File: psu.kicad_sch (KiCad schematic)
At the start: 30 parts, among them U7 LM2593HVS-ADJ, U8 LM2575S-5, U9 LM2575S-3.3

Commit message: More updates to regularise property names
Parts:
- C25: Manuf (none) -> Samsung Electro-Mechanics; Mfr Samsung Electro-Mechanics -> (none); Mfr Part No CL21A475KBQNNNE -> (none); Part (none) -> CL21A475KBQNNNE; Supl Mouser -> (none); Supl Part No 187-CL21A475KBQNNNE -> (none); Supl Price 0.20 -> (none); Vendor (none) -> Mouser; Vendor Cost (none) -> 0.20; Vendor SKU (none) -> 187-CL21A475KBQNNNE
- C26, C27, C28, C50: Manuf (none) -> Samsung Electro-Mechanics; Mfr Samsung Electro-Mechanics -> (none); Mfr Name C0402C104K8R7411 -> (none); Mfr Part Mouser -> (none); Mfr Part No CL21B104KACNNND -> (none); Part 0.016 -> CL21B104KACNNND; Price KEMET -> (none); Repr-Cost C0402C104K8R7411 -> (none); Stock Number Mouser -> (none); Supl Mouser -> (none); Supl Part No 187-CL21B104KACNNND -> (none); Supl Price 0.027 -> (none); Vendor (none) -> Mouser; Vendor Cost (none) -> 0.027; Vendor SKU (none) -> 187-CL21B104KACNNND
- C29, C32, C33: Manuf (none) -> Samsung Electro-Mechanics; Mfr Samsung Electro-Mechanics -> (none); Mfr Part No CL21A475KAQNNNG -> (none); Part (none) -> CL21A475KAQNNNG; Supl Mouser -> (none); Supl Part No 187-CL21A475KAQNNNG -> (none); Supl Price 0.092 -> (none); Vendor (none) -> Mouser; Vendor Cost (none) -> 0.092; Vendor SKU (none) -> 187-CL21A475KAQNNNG
- C30, C31: Manuf (none) -> CDE / Illinois Capacitor; Mfr CDE / Illinois Capacitor -> (none); Mfr Name 476KXM050M -> (none); Mfr Part Mouser -> (none); Mfr Part No 476KXM050M -> (none); Part 0.269 -> 476KXM050M; Price CDE / Illinois Capacitor -> (none); Repr-Cost 476KXM050M -> (none); Stock Number Mouser -> (none); Supl Mouser -> (none); Supl Part No 598-476KXM050M -> (none); Supl Price 0.269 -> (none); Vendor (none) -> Mouser; Vendor Cost (none) -> 0.269; Vendor SKU (none) -> 598-476KXM050M
- C34: Manuf (none) -> Samsung Electro-Mechanics; Mfr Samsung Electro-Mechanics -> (none); Mfr Part No 187-CL31A476MQHNNNE -> (none); Part (none) -> CL31A476MQHNNNE; Supl Mouser -> (none); Supl Part No 187-CL31A476MQHNNNE -> (none); Supl Price 0.262 -> (none); Vendor (none) -> Mouser; Vendor Cost (none) -> 0.262; Vendor SKU (none) -> 187-CL31A476MQHNNNE
- C49: Manuf (none) -> Taiyo Yuden; Mfr Taiyo Yuden -> (none); Mfr Name C0402C104K8R7411 -> (none); Mfr Part Mouser -> (none); Mfr Part No EMK212BJ105KG-T -> (none); Part Mouser -> EMK212BJ105KG-T; Price 80-C0402C104K8R7411 -> (none); Repr-Cost 0.016 -> (none); Stock Number C0402C104K8R7411 -> (none); Supl Mouser -> (none); Supl Part No 963-EMK212BJ105KG-T -> (none); Supl Price 0.016 -> (none); Vendor (none) -> Mouser; Vendor Cost (none) -> 0.016; Vendor SKU (none) -> 963-EMK212BJ105KG-T
- CP3: Manuf (none) -> Nichicon; Mfr Nichicon -> (none); Mfr Part No UPJ1H471MHD -> (none); Part (none) -> UPJ1H471MHD; Supl Mouser -> (none); Supl Part No 647-UPJ1H471MHD -> (none); Supl Price 0.793 -> (none); Vendor (none) -> Mouser; Vendor Cost (none) -> 0.793; Vendor SKU (none) -> 647-UPJ1H471MHD
- CP4: Manuf (none) -> Nichicon; Mfr Nichicon -> (none); Mfr Part No UPJ1E471MPD -> (none); Part (none) -> UPJ1E471MPD; Supl Mouser -> (none); Supl Part No 647-UPJ1E471MPD -> (none); Supl Price 0.549 -> (none); Vendor (none) -> Mouser; Vendor Cost (none) -> 0.549; Vendor SKU (none) -> 647-UPJ1E471MPD
- CP5, CP6: Manuf (none) -> Nichicon; Mfr Nichicon -> (none); Mfr Part No UPJ1A391MPD6 -> (none); Part (none) -> UPJ1A391MPD6; Supl Mouser -> (none); Supl Part No 647-UPJ1A391MPD6 -> (none); Supl Price 0.465 -> (none); Vendor (none) -> Mouser; Vendor Cost (none) -> 0.465; Vendor SKU (none) -> 647-UPJ1A391MPD6
- CP8: Manuf (none) -> YAGEO; Mfr YAGEO -> (none); Mfr Part No SK050M047AZS0611 -> (none); Part (none) -> SK050M047AZS0611; Supl Mouser -> (none); Supl Part No 603-SK050M047AZS0611 -> (none); Supl Price 0.122 -> (none); Vendor (none) -> Mouser; Vendor Cost (none) -> 0.122; Vendor SKU (none) -> 603-SK050M047AZS0611
- D13: Manuf (none) -> Vishay; Manuf Part No PLZ3V6A-G3/H -> (none); Manufacturer Vishay -> (none); Mfr Vishay -> (none); Mfr Part No PLZ3V6A-G3/H -> (none); Part (none) -> PLZ3V6A-G3/H; Supl Mouser -> (none); Supl Part No 78-PLZ3V6A-G3/H -> (none); Supl Price 0.23 -> (none); Supplier Mouser -> (none); Vendor (none) -> Mouser; Vendor Cost (none) -> 0.23; Vendor SKU (none) -> 78-PLZ3V6A-G3/H
- D6: value B140-E3/5AT -> B140-E3; Manuf (none) -> Vishay; Mfr Vishay -> (none); Mfr Part No B140-E3/5AT -> (none); Part (none) -> B140-E3/5AT; Supl Mouser -> (none); Supl Part No 625-B140-E3 -> (none); Supl Price 0.277 -> (none); Vendor (none) -> Mouser; Vendor Cost (none) -> 0.277; Vendor SKU (none) -> 625-B140-E3
- D7, D8: value B140-E3/5AT -> B140-E3; Manuf (none) -> Vishay; Mfr Vishay -> (none); Mfr Part No B140-E3 -> (none); Part (none) -> B140-E3/5AT; Supl Mouser -> (none); Supl Part No 625-B140-E3 -> (none); Supl Price 0.277 -> (none); Vendor (none) -> Mouser; Vendor Cost (none) -> 0.277; Vendor SKU (none) -> 625-B140-E3
- L2: Manuf (none) -> Coilcraft; Mfr Coilcraft -> (none); Mfr Part No MSS1278H-683KED -> (none); Part (none) -> MSS1278H-683KED; Supl Mouser -> (none); Supl Part No 994-MSS1278H-683KED -> (none); Supl Price 2.13 -> (none); Vendor (none) -> Mouser; Vendor Cost (none) -> 2.13; Vendor SKU (none) -> 994-MSS1278H-683KED
- L3, L4: Manuf (none) -> Coilcraft; Mfr Coilcraft -> (none); Mfr Part No MSS1038-104MLC -> (none); Part (none) -> MSS1038-104MLC; Supl Mouser -> (none); Supl Part No 994-MSS1038-104MLC -> (none); Supl Price 1.32 -> (none); Vendor (none) -> Mouser; Vendor Cost (none) -> 1.32; Vendor SKU (none) -> 994-MSS1038-104MLC
- R20: Manuf (none) -> Yageo; Mfr Yageo -> (none); Mfr Part No RC0805FR-134K7L -> (none); Part (none) -> RC0805FR-134K7L; Supl Mouser -> (none); Supl Part No 603-RC0805FR-134K7L -> (none); Supl Price 0.077 -> (none); Vendor (none) -> Mouser; Vendor Cost (none) -> 0.077; Vendor SKU (none) -> 603-RC0805FR-134K7L
- R21, R22: Manuf (none) -> KOA Speer; Mfr KOA Speer -> (none); Mfr Part No RN732ATTD2182D25 -> (none); Part (none) -> RN732ATTD2182D25; Supl Mouser -> (none); Supl Part No 660-RN732ATTD2182D25 -> (none); Supl Price 0.33 -> (none); Vendor (none) -> Mouser; Vendor Cost (none) -> 0.33; Vendor SKU (none) -> 660-RN732ATTD2182D25
- U7: Manuf (none) -> TI; Mfr TI -> (none); Mfr Part No LM2593HVSX-ADJ/NOPB -> (none); Part (none) -> LM2593HVSX-ADJ/NOPB; Supl Mouser -> (none); Supl Part No 926-LM2593HVSXADJNPB -> (none); Supl Price 5.44 -> (none); Vendor (none) -> Mouser; Vendor Cost (none) -> 5.44; Vendor SKU (none) -> 926-LM2593HVSXADJNPB
- U8: Manuf (none) -> onsemi; Mfr onsemi -> (none); Mfr Part No LM2575D2T-5G -> (none); Part (none) -> LM2575D2T-5G; Supl Mouser -> (none); Supl Part No 863-LM2575D2T-5G -> (none); Supl Price 1.99 -> (none); Vendor (none) -> Mouser; Vendor Cost (none) -> 1.99; Vendor SKU (none) -> 863-LM2575D2T-5G
- U9: Manuf (none) -> onsemi; Mfr onsemi -> (none); Mfr Part No LM2575T-3.3G -> (none); Part (none) -> LM2575T-3.3G; Supl Mouser -> (none); Supl Part No 863-LM2575T-3.3G -> (none); Supl Price 1.76 -> (none); Vendor (none) -> Mouser; Vendor Cost (none) -> 1.76; Vendor SKU (none) -> 863-LM2575T-3.3G

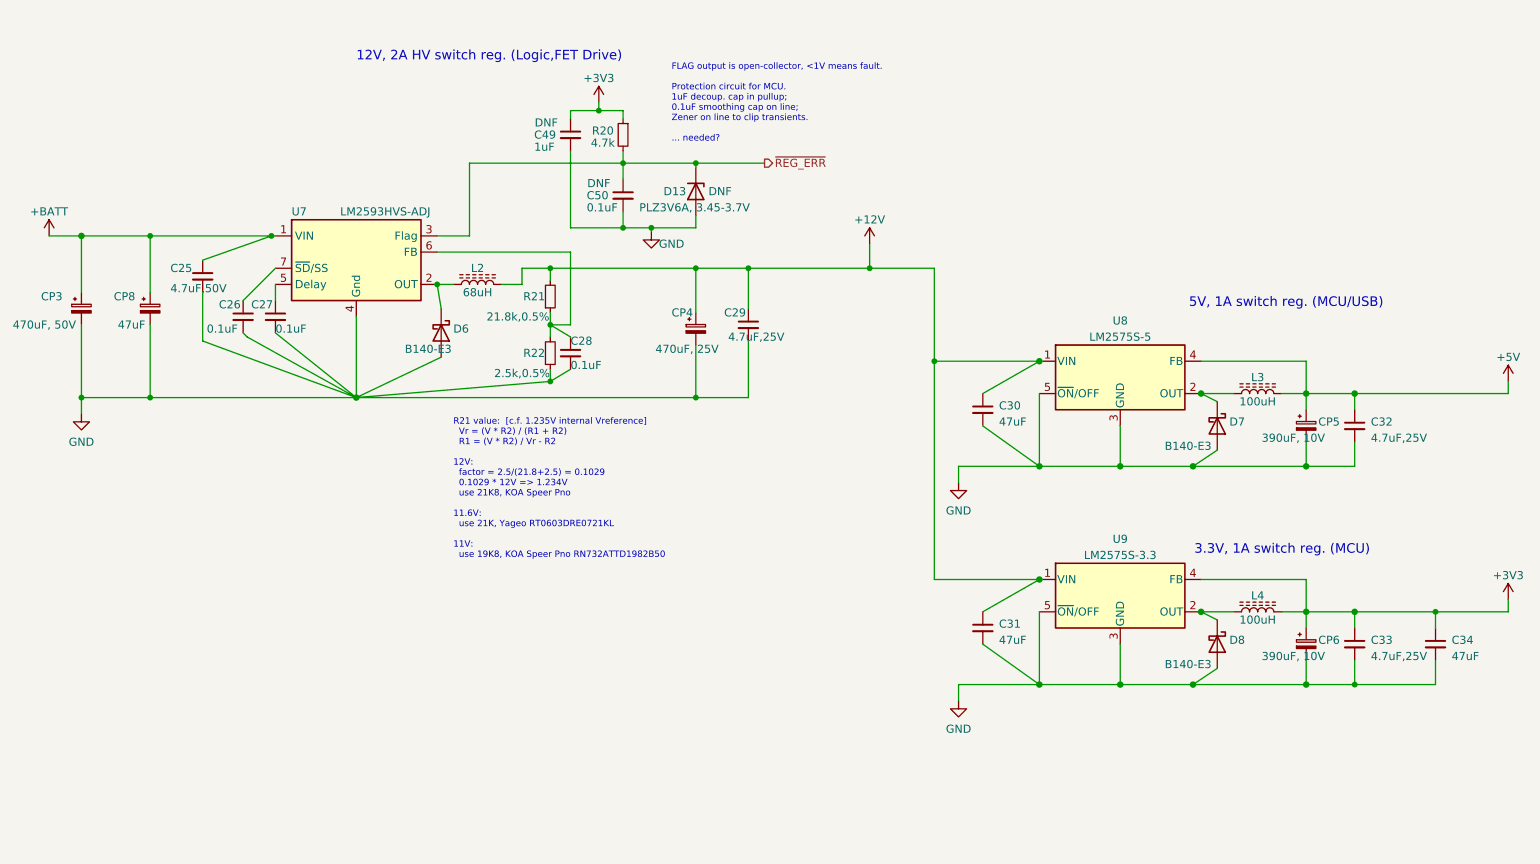
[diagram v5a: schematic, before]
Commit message: Fix some errors in the design (esp net-tie in wrong place)
 - correct led, diode footprints & model
 - fix fuse holder (bad hole spec)
 - update oled mod
 - update EC11 mod
 - add Blender models of case (xz compressed)
 - more updated gerbers (not current!)
 - improve layout of front panel pcb
 - delete unused files
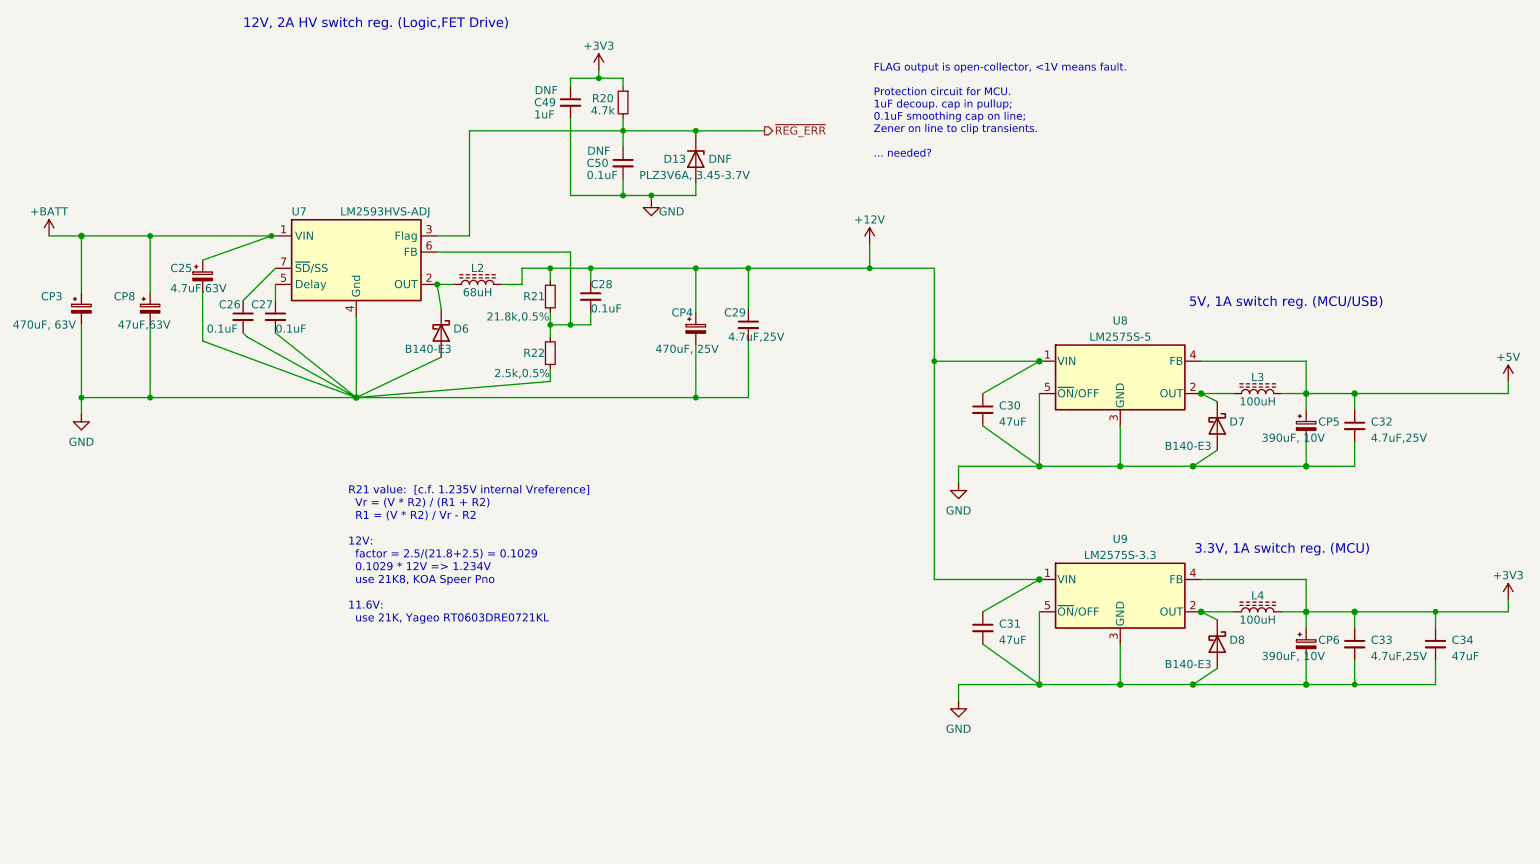
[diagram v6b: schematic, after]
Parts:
- C25: value 4.7uF,50V -> 4.7uF,63V; footprint Capacitor_SMD:C_0805_2012Metric_Pad1.18x1.45mm_HandSolder -> Capacitor_THT:CP_Radial_D5.0mm_P2.00mm; symbol Device:C_Small -> Device:C_Polarized_Small; Manuf Samsung Electro-Mechanics -> Wurth Elektronik; Part CL21A475KBQNNNE -> 860020772008; Vendor Cost 0.20 -> 0.09; Vendor SKU 187-CL21A475KBQNNNE -> 710-860020772008
- CP3: value 470uF, 50V -> 470uF, 63V; Manuf Nichicon -> Panasonic; Part UPJ1H471MHD -> ECA-1JM471; Vendor Cost 0.793 -> 0.807; Vendor SKU 647-UPJ1H471MHD -> 667-ECA-1JM471
- CP4: Manuf Nichicon -> Kemet; Part UPJ1E471MPD -> ESW477M025AH2AA; Vendor Cost 0.549 -> 0.385; Vendor SKU 647-UPJ1E471MPD -> 80-ESW477M025AH2AA
- CP5, CP6: Manuf Nichicon -> Panasonic; Part UPJ1A391MPD6 -> EEU-FC1C391; Vendor Cost 0.465 -> 0.507; Vendor SKU 647-UPJ1A391MPD6 -> 667-EEU-FC1C391
- CP8: value 47uF -> 47uF,63V; Manuf YAGEO -> KEMET; Part SK050M047AZS0611 -> ESK476M063AE3AA; Vendor Cost 0.122 -> 0.246; Vendor SKU 603-SK050M047AZS0611 -> 80-ESK476M063AE3AA
- R22: Manuf KOA Speer -> Susumu; Part RN732ATTD2182D25 -> RR1220P-2491D-M; Vendor Cost 0.33 -> 0.07; Vendor SKU 660-RN732ATTD2182D25 -> 754-RR1220P-2491D-M
- U8: Manuf onsemi -> TI; Part LM2575D2T-5G -> LM2575S-5.0/NOPB; Vendor Cost 1.99 -> 3.77; Vendor SKU 863-LM2575D2T-5G -> 926-LM2575S-5.0/NOPB
- U9: Manuf onsemi -> TI; Part LM2575T-3.3G -> LM2575S-3.3/NOPB; Vendor Cost 1.76 -> 3.77; Vendor SKU 863-LM2575T-3.3G -> 926-LM2575S-3.3/NOPB
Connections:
- net +12V: now also C28.1
- net GND: no longer C28.2
- net at R21.1, R22.2, U7.6 (FB): now also C28.2; no longer C28.1
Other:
- note added: "R21 value: [c.f. 1.235V internal Vreference] Vr = (V * R2) / (R1 + R2) R1 = (V * R2) / Vr - R2 12V: factor = 2.5/(21.8+2.5) = 0.1029 0.1029 * 12V => 1.234V use 21K8, KOA Speer Pno 11.6V: use 21K, Yageo RT0603DRE0721KL"
- note removed: "R21 value: [c.f. 1.235V internal Vreference] Vr = (V * R2) / (R1 + R2) R1 = (V * R2) / Vr - R2 12V: factor = 2.5/(21.8+2.5) = 0.1029 0.1029 * 12V => 1.234V use 21K8, KOA Speer Pno 11.6V: use 21K, Yageo RT0603DRE0721KL 11V: use 19K8, KOA Speer Pno RN732ATTD1982B50"
- moved on the sheet: C28, C49, C50, D13, R20
